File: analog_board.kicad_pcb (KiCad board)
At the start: 2 copper layers, 80 x 80 mm, 53 parts, among them J301 SAMTEC-TSW-105-07-X-D, J302 SAMTEC-TSW-105-07-X-D, J304 SAMTEC-TSW-105-07-X-D, J305 SAMTEC-TSW-105-07-X-D, U1 LM324, U3 AD620, U4 AD620

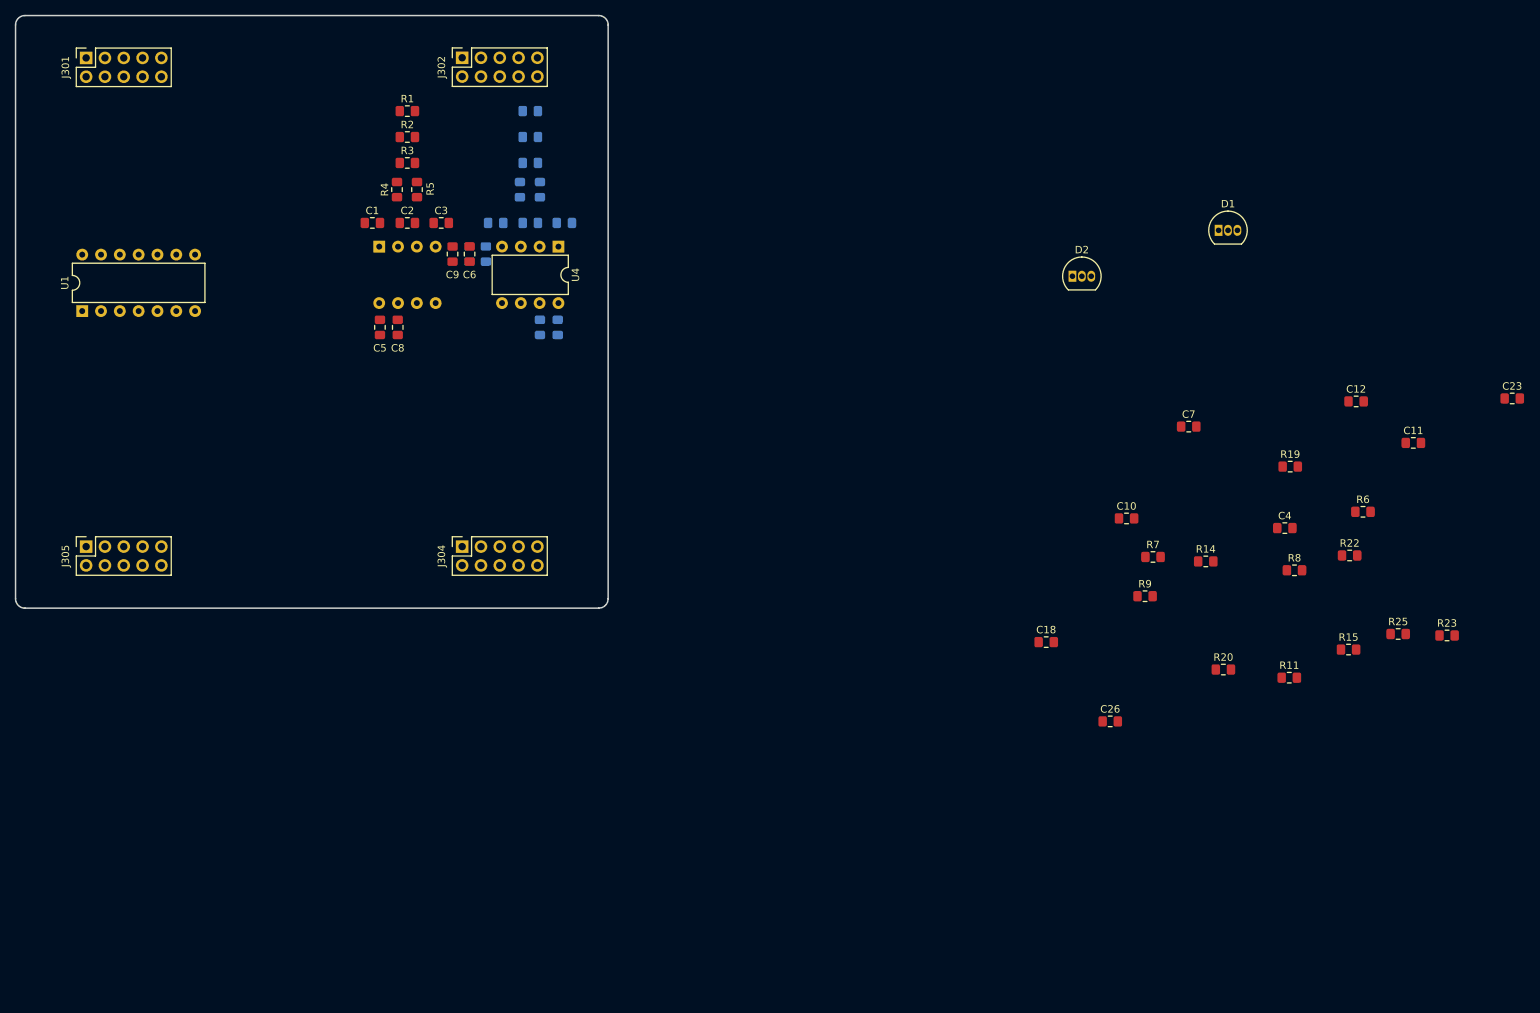
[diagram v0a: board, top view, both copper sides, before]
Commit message: Removed te reference amp of current_ch2, layed out components No wiring yet.
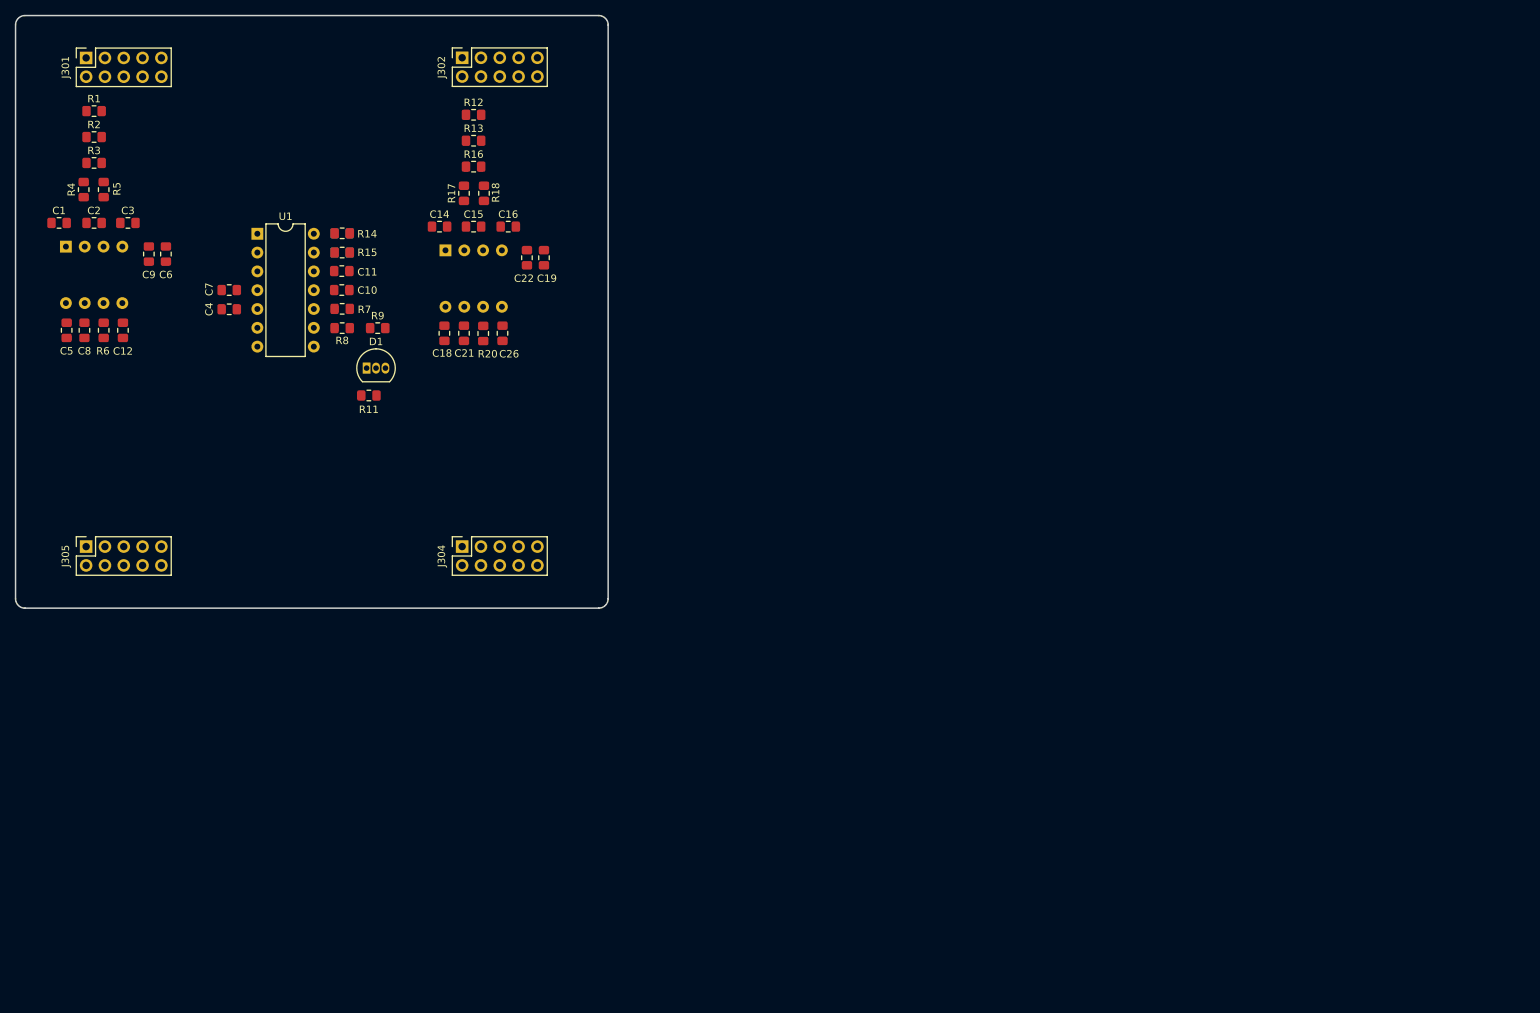
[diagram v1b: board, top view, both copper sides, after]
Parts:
- removed D2: LM385Z-1.2, Package_TO_SOT_THT:TO-92_Inline
- removed R21, R23: 1k, Resistor_SMD:R_0805_2012Metric_Pad1.15x1.40mm_HandSolder
- removed R22: 470R, Resistor_SMD:R_0805_2012Metric_Pad1.15x1.40mm_HandSolder
- removed R25: 3k3, Resistor_SMD:R_0805_2012Metric_Pad1.15x1.40mm_HandSolder
- C14, C15, C16, C19, C21, C22, R12, R13, R16, R17, R18: moved to F.Cu
- C23, R19, U4: moved to B.Cu
- moved R6 171.8 mm to (11.9, 42.5), turned to 90 degrees
- moved C12 166.8 mm to (14.5, 42.5), turned to 90 degrees
- moved C23 159.2 mm to (44.1, 32.0), turned to 180 degrees
- moved C11 146.5 mm to (44.0, 34.5)
- moved R15 146.1 mm to (44.1, 32.0)
- moved C4 145.6 mm to (28.8, 39.7), turned to 180 degrees
- moved R8 132.7 mm to (44.1, 42.2)
- moved R19 131.8 mm to (44.1, 29.4), turned to 180 degrees
- moved C7 130.9 mm to (28.8, 37.1), turned to 180 degrees
- moved R11 130.0 mm to (47.7, 51.3)
- moved R14 124.7 mm to (44.1, 29.4), turned to 180 degrees
- moved D1 116.5 mm to (47.4, 47.6)
- moved R7 114.5 mm to (44.1, 39.6)
- moved C10 110.3 mm to (44.0, 37.1)
- moved R20 109.7 mm to (63.1, 42.9), turned to 270 degrees
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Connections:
- U1 pad 1: Net-(U1-Pad1) -> (no net)
- U1 pad 10: /Torque_pedal_in -> Net-(R7-Pad1)
- U1 pad 12: (no net) -> /Torque_pedal_in
- U1 pad 13: (no net) -> Net-(R19-Pad2)
- U1 pad 14: (no net) -> Net-(R19-Pad2)
- U1 pad 2: Net-(U1-Pad1) -> (no net)
- U1 pad 3: Net-(R7-Pad1) -> (no net)
- U1 pad 5: Net-(R21-Pad1) -> (no net)
- U1 pad 6: Net-(U1-Pad6) -> (no net)
- U1 pad 7: Net-(U1-Pad6) -> (no net)
- U1 pad 8: Net-(R19-Pad2) -> /amp_ref
- U1 pad 9: Net-(R19-Pad2) -> /amp_ref
- U3 pad 5: Net-(U1-Pad1) -> /amp_ref
- U4 pad 5: Net-(U1-Pad6) -> /amp_ref
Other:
- net class Default: clearance 0.2 -> 0.15; trace_width 0.25 -> 0.15
- net class Power added: clearance 0.15, trace_width 0.2, via_dia 0.8, via_drill 0.4
- rule trace_clearance: 0.2 -> 0.15
- rule trace_min: 0.2 -> 0.15

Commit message: Most wiring is done, no ground yet
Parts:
- added R10: 0R, Resistor_SMD:R_1206_3216Metric_Pad1.42x1.75mm_HandSolder, F.Cu at (129.8, 66.0)
- added R21: 0R, Resistor_SMD:R_1206_3216Metric_Pad1.42x1.75mm_HandSolder, F.Cu at (172.8, 107.5)
- C23, R19: moved to F.Cu
- moved C23 144.4 mm to (167.2, 107.6), turned to 90 degrees
- moved R19 143.5 mm to (164.5, 107.6), turned to 90 degrees
- moved C4 140.7 mm to (147.6, 115.2), turned to 270 degrees
- moved C7 140.0 mm to (145.0, 115.2), turned to 270 degrees
- moved U1 133.0 mm to (137.4, 111.4), turned to 90 degrees
- moved J305 126.5 mm to (124.6, 124.2)
- moved C6 122.1 mm to (130.3, 85.2)
- moved C1 122.1 mm to (115.9, 81.0)
- moved C12 122.1 mm to (124.5, 95.5)
- moved C2 122.1 mm to (120.6, 81.0)
- moved C3 122.1 mm to (125.2, 81.0)
- moved C5 122.1 mm to (116.9, 95.5)
- moved C8 122.1 mm to (119.3, 95.5)
- moved C9 122.1 mm to (128.0, 85.2)
- moved R1 122.1 mm to (120.6, 65.9)
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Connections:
- C12 pad 1: /Current_ch1_out -> Net-(C12-Pad1)
- R1 pad 2: /Current_sensor_1 -> Net-(R1-Pad2)
- R2 pad 2: /Current_sensor_1 -> Net-(R1-Pad2)
- R3 pad 2: /Current_sensor_1 -> Net-(R1-Pad2)
- R5 pad 2: /Current_sensor_1 -> Net-(R1-Pad2)
- R6 pad 1: /Current_ch1_out -> Net-(C12-Pad1)
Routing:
- net +15V: track 0.00 -> 157.0 mm
- net -15V: track 0.00 -> 88.8 mm
- net Net-(C12-Pad1): track 0.00 -> 59.0 mm
- net /Current_sensor_1: track 0.00 -> 41.2 mm
- net /Current_ch2_out: track 0.00 -> 30.2 mm
- net Net-(R19-Pad2): track 0.00 -> 28.3 mm
- net /3V3_REF: track 0.00 -> 23.3 mm
- net /Torque_pedal_ADC: track 0.00 -> 19.5 mm
- net /Current_ch1_out: track 0.00 -> 17.1 mm
- net Net-(R1-Pad2): track 0.00 -> 16.4 mm
- net /Current_sensor_2: track 0.00 -> 15.2 mm
- net Net-(C15-Pad2): track 0.00 -> 10.1 mm
- net Net-(C14-Pad2): track 0.00 -> 9.84 mm
- net Net-(D1-Pad2): track 0.00 -> 9.64 mm
- net Net-(C1-Pad2): track 0.00 -> 9.60 mm
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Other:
- net class Current_sensor added: clearance 0.2, trace_width 0.3, via_dia 0.8, via_drill 0.4
- net class Default: clearance 0.15 -> 0.2; trace_width 0.15 -> 0.2
- net class Power: clearance 0.15 -> 0.2; trace_width 0.2 -> 0.3
- rule trace_clearance: 0.15 -> 0.2

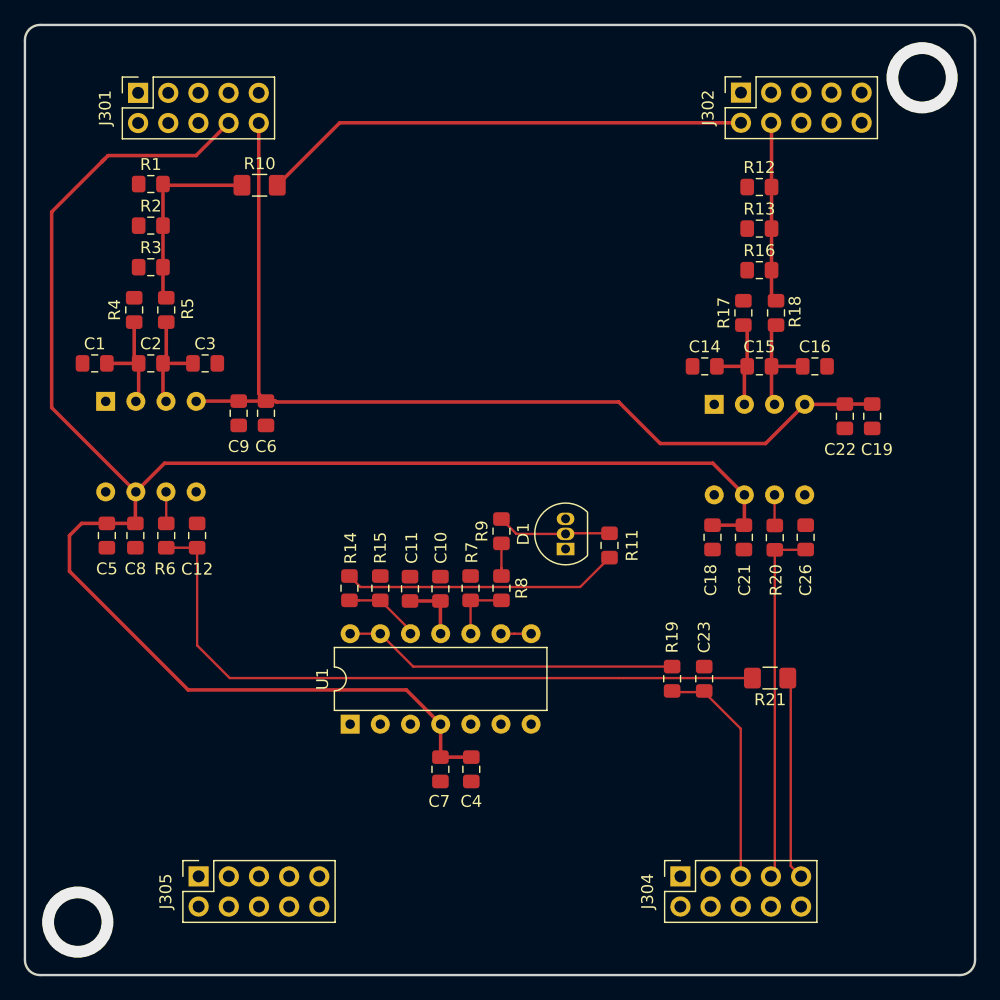
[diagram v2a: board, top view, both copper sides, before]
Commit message: All wiring done, except for grounding
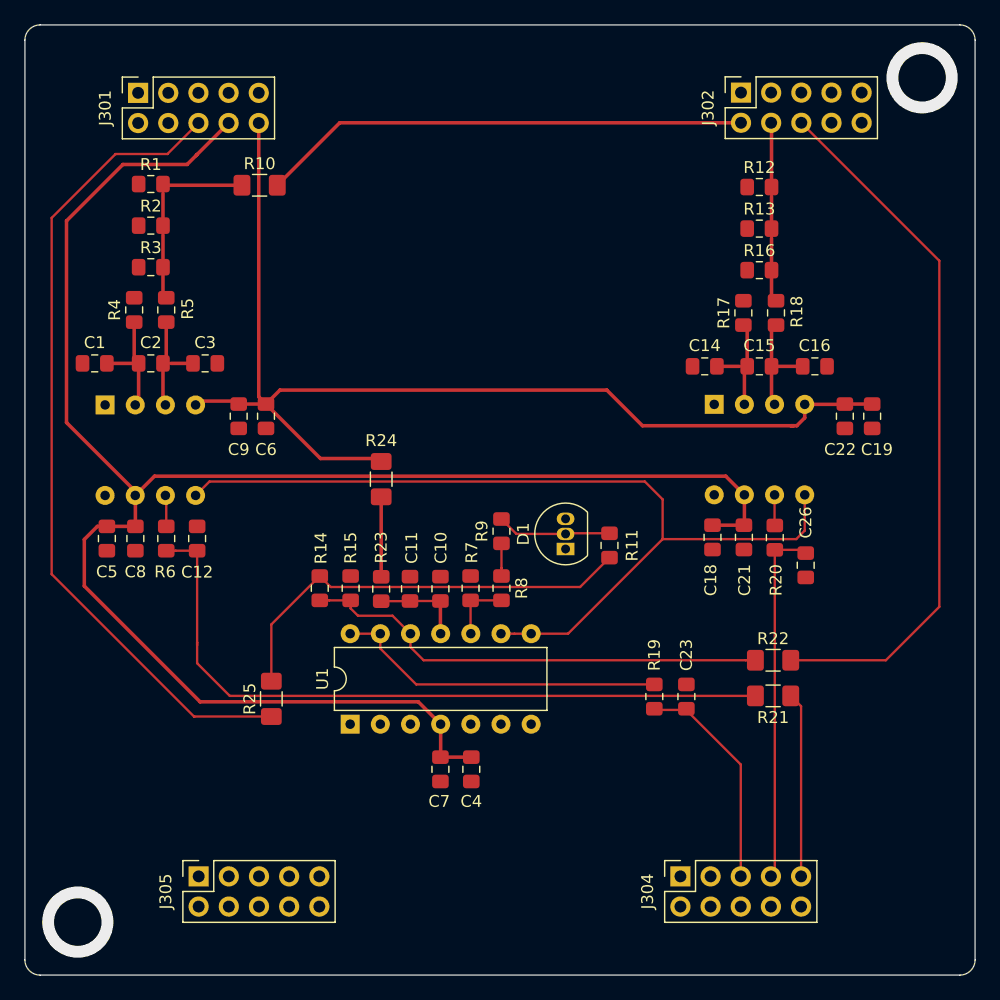
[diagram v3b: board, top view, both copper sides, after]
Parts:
- added R22: 0R, Resistor_SMD:R_1206_3216Metric_Pad1.42x1.75mm_HandSolder, F.Cu at (173.0, 106.0)
- added R23: 0R, Resistor_SMD:R_0805_2012Metric_Pad1.15x1.40mm_HandSolder, F.Cu at (140.0, 100.0)
- added R24: 0R, Resistor_SMD:R_1206_3216Metric_Pad1.42x1.75mm_HandSolder, F.Cu at (140.0, 90.8)
- added R25: 0R, Resistor_SMD:R_1206_3216Metric_Pad1.42x1.75mm_HandSolder, F.Cu at (130.8, 109.2)
- moved R14 2.50 mm to (134.8, 99.9)
- moved R15 2.50 mm to (137.4, 99.9)
- moved C26 2.35 mm to (175.8, 98.0), turned to 270 degrees
- moved C23 2.12 mm to (165.7, 109.1)
- moved R19 2.12 mm to (163.0, 109.1)
- moved R21 1.52 mm to (173.0, 109.0)
- moved U3 0.30 mm to (116.8, 84.5)
- moved C12 0.25 mm to (124.5, 95.8)
- moved C5 0.25 mm to (116.9, 95.8)
- moved C6 0.25 mm to (130.3, 85.5)
- moved C8 0.25 mm to (119.3, 95.8)
- moved C9 0.25 mm to (128.0, 85.5)
- moved R6 0.25 mm to (121.9, 95.8)
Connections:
- R14 pad 1: /3V3_REF -> Net-(R14-Pad1)
- R14 pad 2: /Torque_pedal_in -> Net-(R14-Pad2)
- R15 pad 1: /Torque_pedal_in -> Net-(R14-Pad2)
- U1 pad 12: /Torque_pedal_in -> Net-(R14-Pad2)
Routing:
- net /amp_ref: track 2.54 -> 76.0 mm
- net /3V3_REF: track 23.3 -> 95.0 mm
- net /Torque_pedal_in: track 6.46 -> 59.9 mm
- net Net-(R14-Pad2): track 0.00 -> 40.1 mm
- net -15V: track 88.8 -> 103.2 mm
- net Net-(R14-Pad1): track 0.00 -> 10.1 mm
- net Net-(R23-Pad2): track 0.00 -> 6.99 mm
- net +15V: track 157.0 -> 151.8 mm
- net Net-(C12-Pad1): track 59.0 -> 61.0 mm
- net /Current_ch1_out: track 17.1 -> 15.6 mm
- net /Torque_pedal_ADC: track 19.5 -> 18.7 mm

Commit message: All wiring done, awaiting review
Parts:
- moved R23 0.20 mm to (140.0, 99.8)
- moved C11 0.19 mm to (142.4, 99.8)
- moved C10 0.18 mm to (145.0, 99.8)
- moved R7 0.13 mm to (147.5, 99.8)
- moved R8 0.13 mm to (150.1, 99.8)
- moved R14 0.13 mm to (134.8, 99.8)
- moved R15 0.13 mm to (137.4, 99.8)
- moved R21 0.10 mm to (173.1, 109.0)
- moved R22 0.10 mm to (173.1, 106.0)
- moved R10 0.06 mm to (129.7, 66.0)
- moved C23 0.06 mm to (165.7, 109.0)
- moved R19 0.06 mm to (163.0, 109.0)
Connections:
- R14 pad 1: Net-(R14-Pad1) -> /3V3_REF
- R23 pad 2: Net-(R23-Pad2) -> -15V
- R24 pad 2: Net-(R23-Pad2) -> -15V
- R25 pad 2: Net-(R14-Pad1) -> /3V3_REF
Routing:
- net GND: track 0.00 -> 54.7 mm, vias 0 -> 29
- net /3V3_REF: track 95.0 -> 107.6 mm
- net Net-(R14-Pad1): track 10.1 -> 0.00 mm
- net Net-(R23-Pad2): track 6.99 -> 0.00 mm
- net -15V: track 103.2 -> 110.1 mm
- net /Torque_pedal_in: track 59.9 -> 54.5 mm
- net +15V: track 151.8 -> 152.7 mm
- added copper zone on B.Cu, net GND
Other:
- rule via_min_drill: 0.3 -> 0.4
- rule via_min_size: 0.4 -> 0.55
